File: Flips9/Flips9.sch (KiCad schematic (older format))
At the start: 24 parts, among them CN1 UFP2810

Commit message: Rotate connectors CN1,2
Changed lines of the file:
@@
 L Connector_Generic:Conn_02x08_Odd_Even CND1
 U 1 1 5C8116D8
-P 7650 1325
-F 0 "CND1" H 7700 1842 50  0000 C CNN
-F 1 "Conn_02x08_Odd_Even" H 7700 1751 50  0000 C CNN
-F 2 "Own:Pin_Header_Straight_Shrouded_Locks_2x08_Pitch2.54mm_ConvNumbering" H 7650 1325 50  0001 C CNN
-F 3 "~" H 7650 1325 50  0001 C CNN
-	1    7650 1325
-	1    0    0    -1
+P 7750 1425
+F 0 "CND1" H 7800 1942 50  0000 C CNN
+F 1 "Conn_02x08_Odd_Even" H 7800 1851 50  0000 C CNN
+F 2 "Own:Pin_Header_Straight_Shrouded_Locks_2x08_Pitch2.54mm_ConvNumbering" H 7750 1425 50  0001 C CNN
+F 3 "~" H 7750 1425 50  0001 C CNN
+	1    7750 1425
+	-1   0    0    1
 $EndComp
 $Comp
 L Connector_Generic:Conn_02x08_Odd_Even CND2
 U 1 1 5C81172E
-P 8700 1325
-F 0 "CND2" H 8750 1842 50  0000 C CNN
-F 1 "Conn_02x08_Odd_Even" H 8750 1751 50  0000 C CNN
-F 2 "Own:Pin_Header_Straight_Shrouded_Locks_2x08_Pitch2.54mm_ConvNumbering" H 8700 1325 50  0001 C CNN
-F 3 "~" H 8700 1325 50  0001 C CNN
-	1    8700 1325
-	1    0    0    -1
+P 8800 1425
+F 0 "CND2" H 8850 1942 50  0000 C CNN
+F 1 "Conn_02x08_Odd_Even" H 8850 1851 50  0000 C CNN
+F 2 "Own:Pin_Header_Straight_Shrouded_Locks_2x08_Pitch2.54mm_ConvNumbering" H 8800 1425 50  0001 C CNN
+F 3 "~" H 8800 1425 50  0001 C CNN
+	1    8800 1425
+	-1   0    0    1
 $EndComp
 Text Label 6450 1025 2    50   ~ 0

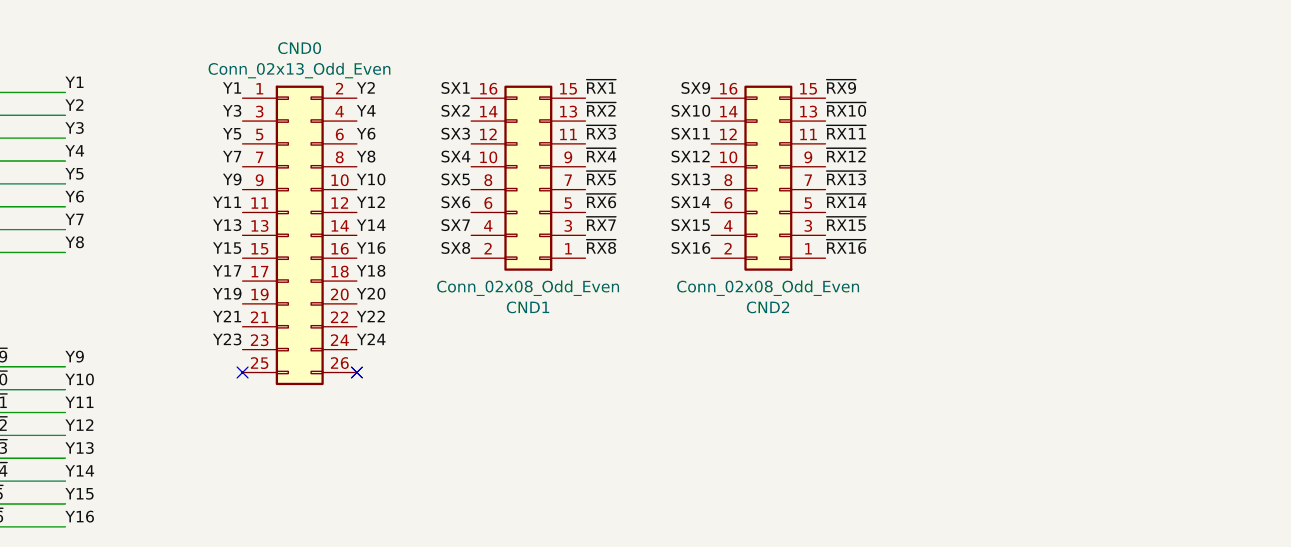
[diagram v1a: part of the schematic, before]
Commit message: adding extra 16 pin connector instead of reusing 24-pin connector
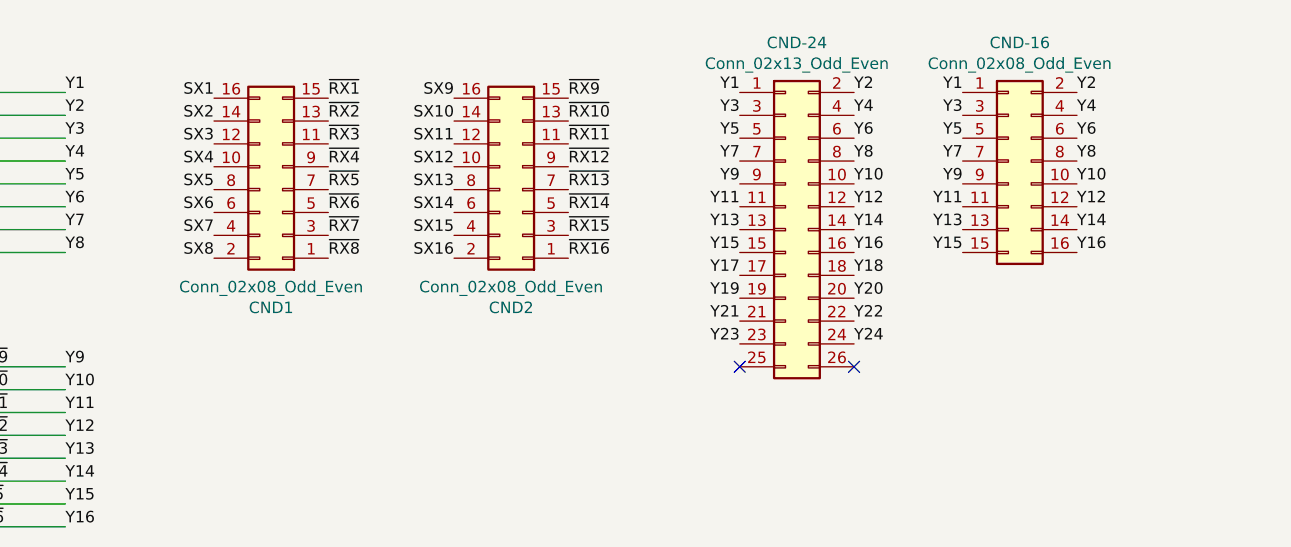
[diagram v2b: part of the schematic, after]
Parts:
- added CND-16: Conn_02x08_Odd_Even, Own:Pin_Header_Straight_Shrouded_Locks_2x08_Pitch2.54mm_ConvNumbering, symbol Connector_Generic:Conn_02x08_Odd_Even
- renumbered CND0 to CND-24
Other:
- moved on the sheet: CND-24, CND1, CND2
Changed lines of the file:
@@
 Y19
 $Comp
-L Connector_Generic:Conn_02x13_Odd_Even CND0
+L Connector_Generic:Conn_02x13_Odd_Even CND-24
 U 1 1 5C811587
-P 6650 1625
-F 0 "CND0" H 6700 2442 50  0000 C CNN
-F 1 "Conn_02x13_Odd_Even" H 6700 2351 50  0000 C CNN
-F 2 "Own:Pin_Header_Straight_Shrouded_Locks_2x13_Pitch2.54mm_ConvNumbering" H 6650 1625 50  0001 C CNN
-F 3 "~" H 6650 1625 50  0001 C CNN
-	1    6650 1625
+P 8825 1600
+F 0 "CND-24" H 8875 2417 50  0000 C CNN
+F 1 "Conn_02x13_Odd_Even" H 8875 2326 50  0000 C CNN
+F 2 "Own:Pin_Header_Straight_Shrouded_Locks_2x13_Pitch2.54mm_ConvNumbering" H 8825 1600 50  0001 C CNN
+F 3 "~" H 8825 1600 50  0001 C CNN
+	1    8825 1600
 	1    0    0    -1
 $EndComp
@@
 L Connector_Generic:Conn_02x08_Odd_Even CND1
 U 1 1 5C8116D8
-P 7750 1425
-F 0 "CND1" H 7800 1942 50  0000 C CNN
-F 1 "Conn_02x08_Odd_Even" H 7800 1851 50  0000 C CNN
-F 2 "Own:Pin_Header_Straight_Shrouded_Locks_2x08_Pitch2.54mm_ConvNumbering" H 7750 1425 50  0001 C CNN
-F 3 "~" H 7750 1425 50  0001 C CNN
-	1    7750 1425
+P 6625 1425
+F 0 "CND1" H 6675 1942 50  0000 C CNN
+F 1 "Conn_02x08_Odd_Even" H 6675 1851 50  0000 C CNN
+F 2 "Own:Pin_Header_Straight_Shrouded_Locks_2x08_Pitch2.54mm_ConvNumbering" H 6625 1425 50  0001 C CNN
+F 3 "~" H 6625 1425 50  0001 C CNN
+	1    6625 1425
 	-1   0    0    1
 $EndComp
@@
 L Connector_Generic:Conn_02x08_Odd_Even CND2
 U 1 1 5C81172E
-P 8800 1425
-F 0 "CND2" H 8850 1942 50  0000 C CNN
-F 1 "Conn_02x08_Odd_Even" H 8850 1851 50  0000 C CNN
-F 2 "Own:Pin_Header_Straight_Shrouded_Locks_2x08_Pitch2.54mm_ConvNumbering" H 8800 1425 50  0001 C CNN
-F 3 "~" H 8800 1425 50  0001 C CNN
-	1    8800 1425
+P 7675 1425
+F 0 "CND2" H 7725 1942 50  0000 C CNN
+F 1 "Conn_02x08_Odd_Even" H 7725 1851 50  0000 C CNN
+F 2 "Own:Pin_Header_Straight_Shrouded_Locks_2x08_Pitch2.54mm_ConvNumbering" H 7675 1425 50  0001 C CNN
+F 3 "~" H 7675 1425 50  0001 C CNN
+	1    7675 1425
 	-1   0    0    1
 $EndComp
-Text Label 6450 1025 2    50   ~ 0
+Text Label 8625 1000 2    50   ~ 0
 Y1
-Text Label 6950 1025 0    50   ~ 0
+Text Label 9125 1000 0    50   ~ 0
 Y2
-Text Label 6450 1125 2    50   ~ 0
+Text Label 8625 1100 2    50   ~ 0
 Y3
-Text Label 6950 1125 0    50   ~ 0
+Text Label 9125 1100 0    50   ~ 0
 Y4
-Text Label 6450 1225 2    50   ~ 0
+Text Label 8625 1200 2    50   ~ 0
 Y5
-Text Label 6950 1225 0    50   ~ 0
+Text Label 9125 1200 0    50   ~ 0
 Y6
-Text Label 6450 1325 2    50   ~ 0
+Text Label 8625 1300 2    50   ~ 0
 Y7
-Text Label 6950 1325 0    50   ~ 0
+Text Label 9125 1300 0    50   ~ 0
 Y8
-Text Label 6450 1425 2    50   ~ 0
+Text Label 8625 1400 2    50   ~ 0
 Y9
-Text Label 6950 1425 0    50   ~ 0
+Text Label 9125 1400 0    50   ~ 0
 Y10
-Text Label 6450 1525 2    50   ~ 0
+Text Label 8625 1500 2    50   ~ 0
 Y11
-Text Label 6950 1525 0    50   ~ 0
+Text Label 9125 1500 0    50   ~ 0
 Y12
-Text Label 6450 1625 2    50   ~ 0
+Text Label 8625 1600 2    50   ~ 0
 Y13
-Text Label 6950 1625 0    50   ~ 0
+Text Label 9125 1600 0    50   ~ 0
 Y14
-Text Label 6450 1725 2    50   ~ 0
+Text Label 8625 1700 2    50   ~ 0
 Y15
-Text Label 6950 1725 0    50   ~ 0
+Text Label 9125 1700 0    50   ~ 0
 Y16
-Text Label 6950 2025 0    50   ~ 0
+Text Label 9125 2000 0    50   ~ 0
 Y22
-Text Label 6950 2125 0    50   ~ 0
+Text Label 9125 2100 0    50   ~ 0
 Y24
-Text Label 6950 1825 0    50   ~ 0
+Text Label 9125 1800 0    50   ~ 0
 Y18
-Text Label 6950 1925 0    50   ~ 0
+Text Label 9125 1900 0    50   ~ 0
 Y20
-Text Label 6450 2025 2    50   ~ 0
+Text Label 8625 2000 2    50   ~ 0
 Y21
-Text Label 6450 2125 2    50   ~ 0
+Text Label 8625 2100 2    50   ~ 0
 Y23
-Text Label 6450 1825 2    50   ~ 0
+Text Label 8625 1800 2    50   ~ 0
 Y17
-Text Label 6450 1925 2    50   ~ 0
+Text Label 8625 1900 2    50   ~ 0
 Y19
-NoConn ~ 6450 2225
-NoConn ~ 6950 2225
-Text Label 7450 1025 2    50   ~ 0
+NoConn ~ 8625 2200
+NoConn ~ 9125 2200
+Text Label 6325 1025 2    50   ~ 0
 SX1
-Text Label 7450 1225 2    50   ~ 0
+Text Label 6325 1225 2    50   ~ 0
 SX3
-Text Label 7450 1425 2    50   ~ 0
+Text Label 6325 1425 2    50   ~ 0
 SX5
-Text Label 7450 1625 2    50   ~ 0
+Text Label 6325 1625 2    50   ~ 0
 SX7
-Text Label 7450 1125 2    50   ~ 0
+Text Label 6325 1125 2    50   ~ 0
 SX2
-Text Label 7450 1325 2    50   ~ 0
+Text Label 6325 1325 2    50   ~ 0
 SX4
-Text Label 7450 1525 2    50   ~ 0
+Text Label 6325 1525 2    50   ~ 0
 SX6
-Text Label 7450 1725 2    50   ~ 0
+Text Label 6325 1725 2    50   ~ 0
 SX8
-Text Label 8500 1625 2    50   ~ 0
+Text Label 7375 1625 2    50   ~ 0
 SX15
-Text Label 8500 1725 2    50   ~ 0
+Text Label 7375 1725 2    50   ~ 0
 SX16
-Text Label 8500 1025 2    50   ~ 0
+Text Label 7375 1025 2    50   ~ 0
 SX9
-Text Label 8500 1225 2    50   ~ 0
+Text Label 7375 1225 2    50   ~ 0
 SX11
-Text Label 8500 1425 2    50   ~ 0
+Text Label 7375 1425 2    50   ~ 0
 SX13
-Text Label 8500 1125 2    50   ~ 0
+Text Label 7375 1125 2    50   ~ 0
 SX10
-Text Label 8500 1325 2    50   ~ 0
+Text Label 7375 1325 2    50   ~ 0
 SX12
-Text Label 8500 1525 2    50   ~ 0
+Text Label 7375 1525 2    50   ~ 0
 SX14
-Text Label 9000 1725 0    50   ~ 0
+Text Label 7875 1725 0    50   ~ 0
 ~RX16
-Text Label 9000 1625 0    50   ~ 0
+Text Label 7875 1625 0    50   ~ 0
 ~RX15
-Text Label 7950 1125 0    50   ~ 0
+Text Label 6825 1125 0    50   ~ 0
 ~RX2
-Text Label 7950 1325 0    50   ~ 0
+Text Label 6825 1325 0    50   ~ 0
 ~RX4
-Text Label 7950 1525 0    50   ~ 0
+Text Label 6825 1525 0    50   ~ 0
 ~RX6
-Text Label 7950 1725 0    50   ~ 0
+Text Label 6825 1725 0    50   ~ 0
 ~RX8
-Text Label 9000 1125 0    50   ~ 0
+Text Label 7875 1125 0    50   ~ 0
 ~RX10
-Text Label 9000 1325 0    50   ~ 0
+Text Label 7875 1325 0    50   ~ 0
 ~RX12
-Text Label 9000 1525 0    50   ~ 0
+Text Label 7875 1525 0    50   ~ 0
 ~RX14
-Text Label 7950 1025 0    50   ~ 0
+Text Label 6825 1025 0    50   ~ 0
 ~RX1
-Text Label 7950 1225 0    50   ~ 0
+Text Label 6825 1225 0    50   ~ 0
 ~RX3
-Text Label 7950 1425 0    50   ~ 0
+Text Label 6825 1425 0    50   ~ 0
 ~RX5
-Text Label 7950 1625 0    50   ~ 0
+Text Label 6825 1625 0    50   ~ 0
 ~RX7
-Text Label 9000 1025 0    50   ~ 0
+Text Label 7875 1025 0    50   ~ 0
 ~RX9
-Text Label 9000 1225 0    50   ~ 0
+Text Label 7875 1225 0    50   ~ 0
 ~RX11
-Text Label 9000 1425 0    50   ~ 0
+Text Label 7875 1425 0    50   ~ 0
 ~RX13
+$Comp
+L Connector_Generic:Conn_02x08_Odd_Even CND-16
+U 1 1 5C7D9732
+P 9800 1300
+F 0 "CND-16" H 9850 1817 50  0000 C CNN
+F 1 "Conn_02x08_Odd_Even" H 9850 1726 50  0000 C CNN
+F 2 "Own:Pin_Header_Straight_Shrouded_Locks_2x08_Pitch2.54mm_ConvNumbering" H 9800 1300 50  0001 C CNN
+F 3 "~" H 9800 1300 50  0001 C CNN
+	1    9800 1300
+	1    0    0    -1
+$EndComp
+Text Label 9600 1000 2    50   ~ 0
+Y1
+Text Label 9600 1100 2    50   ~ 0
+Y3
+Text Label 9600 1200 2    50   ~ 0
+Y5
+Text Label 9600 1300 2    50   ~ 0
+Y7
+Text Label 9600 1400 2    50   ~ 0
+Y9
+Text Label 9600 1500 2    50   ~ 0
+Y11
+Text Label 9600 1600 2    50   ~ 0
+Y13
+Text Label 9600 1700 2    50   ~ 0
+Y15
+Text Label 10100 1000 0    50   ~ 0
+Y2
+Text Label 10100 1100 0    50   ~ 0
+Y4
+Text Label 10100 1200 0    50   ~ 0
+Y6
+Text Label 10100 1300 0    50   ~ 0
+Y8
+Text Label 10100 1400 0    50   ~ 0
+Y10
+Text Label 10100 1500 0    50   ~ 0
+Y12
+Text Label 10100 1600 0    50   ~ 0
+Y14
+Text Label 10100 1700 0    50   ~ 0
+Y16
 $EndSCHEMATC

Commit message: adding rows 25-32
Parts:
- added CND-162: Conn_02x08_Odd_Even, Own:Pin_Header_Straight_Shrouded_Locks_2x08_Pitch2.54mm_ConvNumbering, symbol Connector_Generic:Conn_02x08_Odd_Even
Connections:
- net labels added: Y25, Y26, Y27, Y28, Y29, Y30, Y31, Y32
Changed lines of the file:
@@
 $Descr A4 11693 8268
 encoding utf-8
-Sheet 1 5
+Sheet 1 6
 Title ""
 Date ""
@@
 $EndDescr
 $Sheet
-S 2775 975  550  3100
+S 2775 975  550  3975
 U 5C4DA960
 F0 "UnitY" 50
 F1 "Unit.sch" 50
-F2 "DATA" I R 3325 3575 50
-F3 "A0" I L 2775 3925 50
-F4 "A1" I L 2775 3725 50
-F5 "A2" I L 2775 3825 50
-F6 "EN" I R 3325 3975 50
-F7 "B0" I R 3325 3725 50
-F8 "B1" I R 3325 3825 50
+F2 "DATA" I R 3325 4425 50
+F3 "A0" I L 2775 4775 50
+F4 "A1" I L 2775 4575 50
+F5 "A2" I L 2775 4675 50
+F6 "EN" I R 3325 4825 50
+F7 "B0" I R 3325 4575 50
+F8 "B1" I R 3325 4675 50
 F9 "0AL" O L 2775 1125 50
 F10 "0BL" O L 2775 1225 50
@@
 F55 "2GH" O R 3325 3425 50
 F56 "20H" O R 3325 2725 50
+F57 "3AL" O L 2775 3675 50
+F58 "3BL" O L 2775 3775 50
+F59 "3CL" O L 2775 3875 50
+F60 "3DL" O L 2775 3975 50
+F61 "3EL" O L 2775 4075 50
+F62 "3FL" O L 2775 4175 50
+F63 "3GL" O L 2775 4275 50
+F64 "30L" O L 2775 3575 50
+F65 "3AH" O R 3325 3675 50
+F66 "3BH" O R 3325 3775 50
+F67 "3CH" O R 3325 3875 50
+F68 "3DH" O R 3325 3975 50
+F69 "3EH" O R 3325 4075 50
+F70 "3FH" O R 3325 4175 50
+F71 "3GH" O R 3325 4275 50
+F72 "30H" O R 3325 3575 50
 $EndSheet
 $Comp
 L Eigene~Bauteile:UFP2810 CN1
 U 1 1 5C58B899
-P 3325 4875
-F 0 "CN1" V 3275 4275 50  0000 L CNN
-F 1 "UFP2810" V 3375 4225 50  0000 L CNN
-F 2 "Own:Pin_Header_Angle_Shrouded_2x05_Pitch2.54mm_ConvNumbering" H 3325 4875 50  0001 C CNN
-F 3 "" H 3325 4875 50  0001 C CNN
-	1    3325 4875
+P 3325 5725
+F 0 "CN1" V 3275 5125 50  0000 L CNN
+F 1 "UFP2810" V 3375 5075 50  0000 L CNN
+F 2 "Own:Pin_Header_Angle_Shrouded_2x05_Pitch2.54mm_ConvNumbering" H 3325 5725 50  0001 C CNN
+F 3 "" H 3325 5725 50  0001 C CNN
+	1    3325 5725
 	0    1    1    0
 $EndComp
 Wire Wire Line
-	3125 4425 3125 4525
-Wire Wire Line
-	3225 5375 3225 5225
-Wire Wire Line
-	3125 5325 3125 5225
-Wire Wire Line
-	3525 5225 3525 5325
-Wire Wire Line
-	3525 5325 3775 5325
-Wire Wire Line
-	3425 5225 3425 5375
-Wire Wire Line
-	3425 5375 3825 5375
-Wire Wire Line
-	2775 3925 2675 3925
-Wire Wire Line
-	2675 3925 2675 4425
-Wire Wire Line
-	2675 4425 3125 4425
-Wire Wire Line
-	2775 3825 2625 3825
-Wire Wire Line
-	2625 3825 2625 5325
-Wire Wire Line
-	2625 5325 3125 5325
-Wire Wire Line
-	2575 5375 2575 3725
-Wire Wire Line
-	2575 3725 2775 3725
-Wire Wire Line
-	2575 5375 3225 5375
-Wire Wire Line
-	3325 3975 3425 3975
-Wire Wire Line
-	3525 3825 3325 3825
-Wire Wire Line
-	3325 3725 3775 3725
-Wire Wire Line
-	3775 3725 3775 5325
-Wire Wire Line
-	3825 5375 3825 3575
-Wire Wire Line
-	3825 3575 3325 3575
-Wire Wire Line
-	3525 3825 3525 4525
-Wire Wire Line
-	3425 3975 3425 4525
+	3125 5275 3125 5375
+Wire Wire Line
+	3225 6225 3225 6075
+Wire Wire Line
+	3125 6175 3125 6075
+Wire Wire Line
+	3525 6075 3525 6175
+Wire Wire Line
+	3525 6175 3775 6175
+Wire Wire Line
+	3425 6075 3425 6225
+Wire Wire Line
+	3425 6225 3825 6225
+Wire Wire Line
+	2775 4775 2675 4775
+Wire Wire Line
+	2675 4775 2675 5275
+Wire Wire Line
+	2675 5275 3125 5275
+Wire Wire Line
+	2775 4675 2625 4675
+Wire Wire Line
+	2625 4675 2625 6175
+Wire Wire Line
+	2625 6175 3125 6175
+Wire Wire Line
+	2575 6225 2575 4575
+Wire Wire Line
+	2575 4575 2775 4575
+Wire Wire Line
+	2575 6225 3225 6225
+Wire Wire Line
+	3325 4825 3425 4825
+Wire Wire Line
+	3525 4675 3325 4675
+Wire Wire Line
+	3325 4575 3775 4575
+Wire Wire Line
+	3775 4575 3775 6175
+Wire Wire Line
+	3825 6225 3825 4425
+Wire Wire Line
+	3825 4425 3325 4425
+Wire Wire Line
+	3525 4675 3525 5375
+Wire Wire Line
+	3425 4825 3425 5375
 Text Label 5675 1000 0    50   ~ 0
 Y1
@@
 L power:VCC #PWR0104
 U 1 1 5C6CC272
-P 3225 4525
-F 0 "#PWR0104" H 3225 4375 50  0001 C CNN
-F 1 "VCC" H 3242 4698 50  0000 C CNN
-F 2 "" H 3225 4525 50  0001 C CNN
-F 3 "" H 3225 4525 50  0001 C CNN
-	1    3225 4525
+P 3225 5375
+F 0 "#PWR0104" H 3225 5225 50  0001 C CNN
+F 1 "VCC" H 3242 5548 50  0000 C CNN
+F 2 "" H 3225 5375 50  0001 C CNN
+F 3 "" H 3225 5375 50  0001 C CNN
+	1    3225 5375
 	1    0    0    -1
 $EndComp
@@
 L power:GND #PWR0105
 U 1 1 5C6CC278
-P 3325 5225
-F 0 "#PWR0105" H 3325 4975 50  0001 C CNN
-F 1 "GND" H 3330 5052 50  0000 C CNN
-F 2 "" H 3325 5225 50  0001 C CNN
-F 3 "" H 3325 5225 50  0001 C CNN
-	1    3325 5225
+P 3325 6075
+F 0 "#PWR0105" H 3325 5825 50  0001 C CNN
+F 1 "GND" H 3330 5902 50  0000 C CNN
+F 2 "" H 3325 6075 50  0001 C CNN
+F 3 "" H 3325 6075 50  0001 C CNN
+	1    3325 6075
 	1    0    0    -1
 $EndComp
@@
 L power:+24V #PWR0106
 U 1 1 5C6CC27E
-P 3325 4525
-F 0 "#PWR0106" H 3325 4375 50  0001 C CNN
-F 1 "+24V" H 3340 4698 50  0000 C CNN
-F 2 "" H 3325 4525 50  0001 C CNN
-F 3 "" H 3325 4525 50  0001 C CNN
-	1    3325 4525
+P 3325 5375
+F 0 "#PWR0106" H 3325 5225 50  0001 C CNN
+F 1 "+24V" H 3340 5548 50  0000 C CNN
+F 2 "" H 3325 5375 50  0001 C CNN
+F 3 "" H 3325 5375 50  0001 C CNN
+	1    3325 5375
 	1    0    0    -1
 $EndComp
@@
 Text Label 10100 1700 0    50   ~ 0
 Y16
+$Comp
+L Connector_Generic:Conn_02x08_Odd_Even CND-162
+U 1 1 5C82CFBD
+P 9800 2350
+F 0 "CND-162" H 9850 2867 50  0000 C CNN
+F 1 "Conn_02x08_Odd_Even" H 9850 2776 50  0000 C CNN
+F 2 "Own:Pin_Header_Straight_Shrouded_Locks_2x08_Pitch2.54mm_ConvNumbering" H 9800 2350 50  0001 C CNN
+F 3 "~" H 9800 2350 50  0001 C CNN
+	1    9800 2350
+	1    0    0    -1
+$EndComp
+Text Label 10100 2250 0    50   ~ 0
+Y22
+Text Label 10100 2350 0    50   ~ 0
+Y24
+Text Label 10100 2050 0    50   ~ 0
+Y18
+Text Label 10100 2150 0    50   ~ 0
+Y20
+Text Label 9600 2250 2    50   ~ 0
+Y21
+Text Label 9600 2350 2    50   ~ 0
+Y23
+Text Label 9600 2050 2    50   ~ 0
+Y17
+Text Label 9600 2150 2    50   ~ 0
+Y19
+Text Label 10100 2450 0    50   ~ 0
+Y26
+Text Label 10100 2550 0    50   ~ 0
+Y28
+Text Label 10100 2650 0    50   ~ 0
+Y30
+Text Label 10100 2750 0    50   ~ 0
+Y32
+Text Label 9600 2450 2    50   ~ 0
+Y25
+Text Label 9600 2550 2    50   ~ 0
+Y27
+Text Label 9600 2650 2    50   ~ 0
+Y29
+Text Label 9600 2750 2    50   ~ 0
+Y31
+Text Label 3325 3575 0    50   ~ 0
+Y25
+Text Label 3325 3675 0    50   ~ 0
+Y26
+Text Label 3325 3775 0    50   ~ 0
+Y27
+Text Label 3325 3875 0    50   ~ 0
+Y28
+Text Label 3325 3975 0    50   ~ 0
+Y29
+Text Label 3325 4075 0    50   ~ 0
+Y30
+Text Label 3325 4175 0    50   ~ 0
+Y31
+Text Label 3325 4275 0    50   ~ 0
+Y32
+Text Label 2775 3575 2    50   ~ 0
+Y25
+Text Label 2775 3675 2    50   ~ 0
+Y26
+Text Label 2775 3775 2    50   ~ 0
+Y27
+Text Label 2775 3875 2    50   ~ 0
+Y28
+Text Label 2775 3975 2    50   ~ 0
+Y29
+Text Label 2775 4075 2    50   ~ 0
+Y30
+Text Label 2775 4175 2    50   ~ 0
+Y31
+Text Label 2775 4275 2    50   ~ 0
+Y32
 $EndSCHEMATC

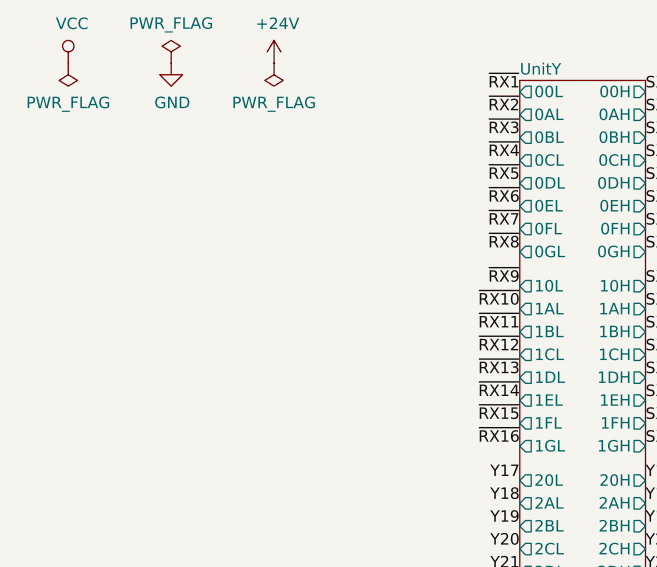
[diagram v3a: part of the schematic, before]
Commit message: Adding capacitors, moving main decoder
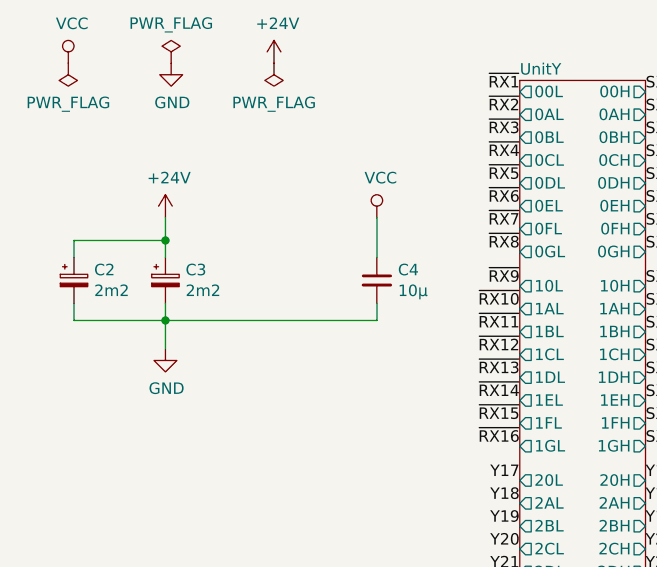
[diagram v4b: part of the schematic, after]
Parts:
- added C2, C3: 2m2, Capacitors_THT:CP_Radial_D13.0mm_P5.00mm, symbol Device:CP_Small
- added C4: 10µ, Capacitors_SMD:C_0805_HandSoldering, symbol Device:C_Small
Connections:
- wire segments 56 -> 67
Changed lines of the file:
@@
 Text Label 2775 4275 2    50   ~ 0
 Y32
+$Comp
+L Device:CP_Small C3
+U 1 1 5C867916
+P 1225 1850
+F 0 "C3" H 1313 1896 50  0000 L CNN
+F 1 "2m2" H 1313 1805 50  0000 L CNN
+F 2 "Capacitors_THT:CP_Radial_D13.0mm_P5.00mm" H 1225 1850 50  0001 C CNN
+F 3 "~" H 1225 1850 50  0001 C CNN
+	1    1225 1850
+	1    0    0    -1
+$EndComp
+$Comp
+L Device:CP_Small C2
+U 1 1 5C867F99
+P 825 1850
+F 0 "C2" H 913 1896 50  0000 L CNN
+F 1 "2m2" H 913 1805 50  0000 L CNN
+F 2 "Capacitors_THT:CP_Radial_D13.0mm_P5.00mm" H 825 1850 50  0001 C CNN
+F 3 "~" H 825 1850 50  0001 C CNN
+	1    825  1850
+	1    0    0    -1
+$EndComp
+Wire Wire Line
+	825  1750 825  1675
+Wire Wire Line
+	825  1675 1225 1675
+Wire Wire Line
+	1225 1750 1225 1675
+Connection ~ 1225 1675
+Wire Wire Line
+	825  1950 825  2025
+Wire Wire Line
+	825  2025 1225 2025
+Wire Wire Line
+	1225 1950 1225 2025
+Connection ~ 1225 2025
+$Comp
+L power:GND #PWR0107
+U 1 1 5C870124
+P 1225 2150
+F 0 "#PWR0107" H 1225 1900 50  0001 C CNN
+F 1 "GND" H 1230 1977 50  0000 C CNN
+F 2 "" H 1225 2150 50  0001 C CNN
+F 3 "" H 1225 2150 50  0001 C CNN
+	1    1225 2150
+	1    0    0    -1
+$EndComp
+Wire Wire Line
+	1225 2025 1225 2150
+$Comp
+L power:+24V #PWR0108
+U 1 1 5C87016B
+P 1225 1575
+F 0 "#PWR0108" H 1225 1425 50  0001 C CNN
+F 1 "+24V" H 1240 1748 50  0000 C CNN
+F 2 "" H 1225 1575 50  0001 C CNN
+F 3 "" H 1225 1575 50  0001 C CNN
+	1    1225 1575
+	1    0    0    -1
+$EndComp
+Wire Wire Line
+	1225 1575 1225 1675
+$Comp
+L Device:C_Small C4
+U 1 1 5C876CE2
+P 2150 1850
+F 0 "C4" H 2242 1896 50  0000 L CNN
+F 1 "10µ" H 2242 1805 50  0000 L CNN
+F 2 "Capacitors_SMD:C_0805_HandSoldering" H 2150 1850 50  0001 C CNN
+F 3 "~" H 2150 1850 50  0001 C CNN
+	1    2150 1850
+	1    0    0    -1
+$EndComp
+Wire Wire Line
+	1225 2025 2150 2025
+Wire Wire Line
+	2150 2025 2150 1950
+$Comp
+L power:VCC #PWR01
+U 1 1 5C878567
+P 2150 1575
+F 0 "#PWR01" H 2150 1425 50  0001 C CNN
+F 1 "VCC" H 2167 1748 50  0000 C CNN
+F 2 "" H 2150 1575 50  0001 C CNN
+F 3 "" H 2150 1575 50  0001 C CNN
+	1    2150 1575
+	1    0    0    -1
+$EndComp
+Wire Wire Line
+	2150 1575 2150 1750
 $EndSCHEMATC
